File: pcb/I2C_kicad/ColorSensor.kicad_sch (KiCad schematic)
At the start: 0 parts

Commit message: started working on color sensor
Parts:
- added C2: 100nF, Capacitor_SMD:C_0603_1608Metric, symbol Device:C
- added R1, R2: 2.2kΩ, Resistor_SMD:R_0603_1608Metric, symbol Device:R
- added U1: VEML3328, SMD_L3328_VIS, symbol VEML3328:VEML3328
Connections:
- new net +3V3: C2.1, U1.4
- new net GND: C2.2, U1.1

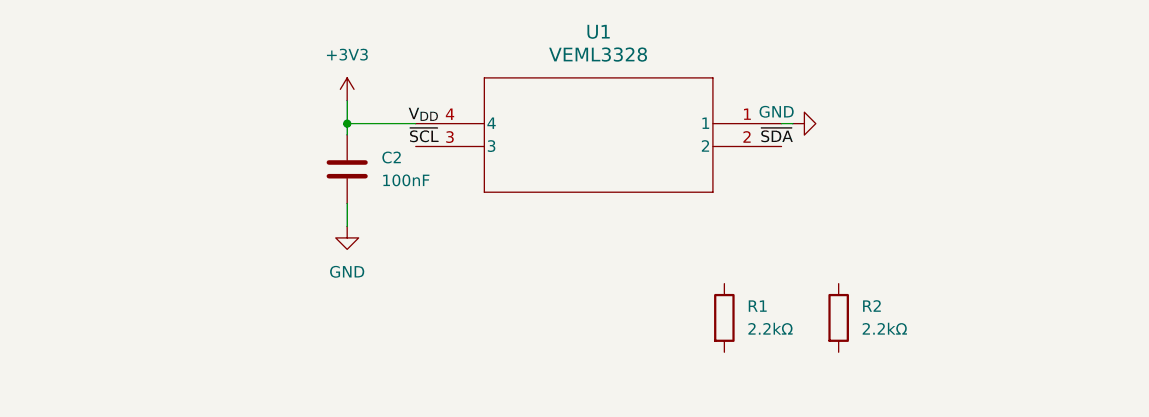
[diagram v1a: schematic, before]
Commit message: I worked on the color sensor and also the gpio expander. I added the pull ups for the SDA and SCL on the color sensor so no need to add any more. Just put do not populate for the other I2c devices
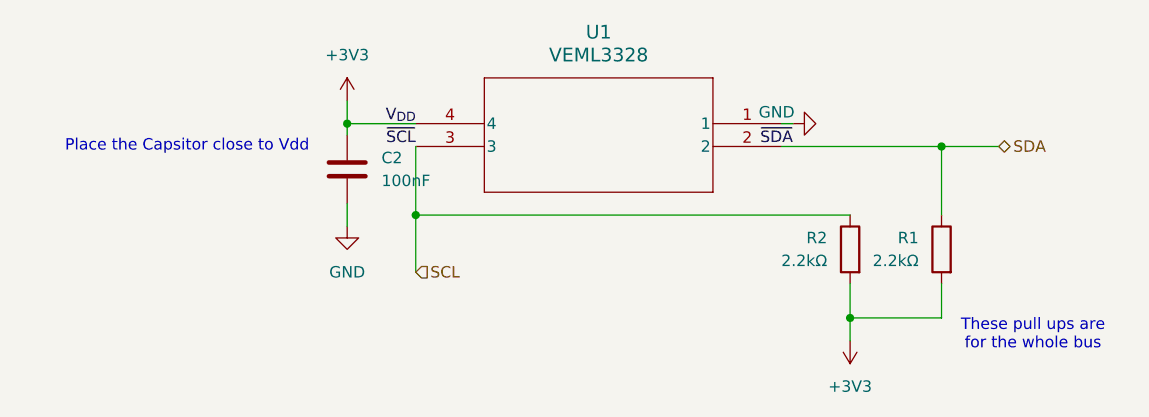
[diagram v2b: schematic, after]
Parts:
- U1: footprint SMD_L3328_VIS -> VEML3328:SMD_L3328_VIS; Manufacturer P/N 751-VEML3328TR-ND -> VEML3328
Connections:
- net +3V3: now also R1.2, R2.2
- net SDA: now reaches R1.1
- net SDA: now also U1.2
- net SCL: now reaches U1.3
- net SCL: now also R2.1
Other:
- note added: "Place the Capsitor close to Vdd"
- note added: "These pull ups are for the whole bus"
- company: (none) -> RoboCup
- title: (none) -> Color Sensor
- moved on the sheet: R1, R2

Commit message: Add IMU, Hall effect, and temp sensor sheets
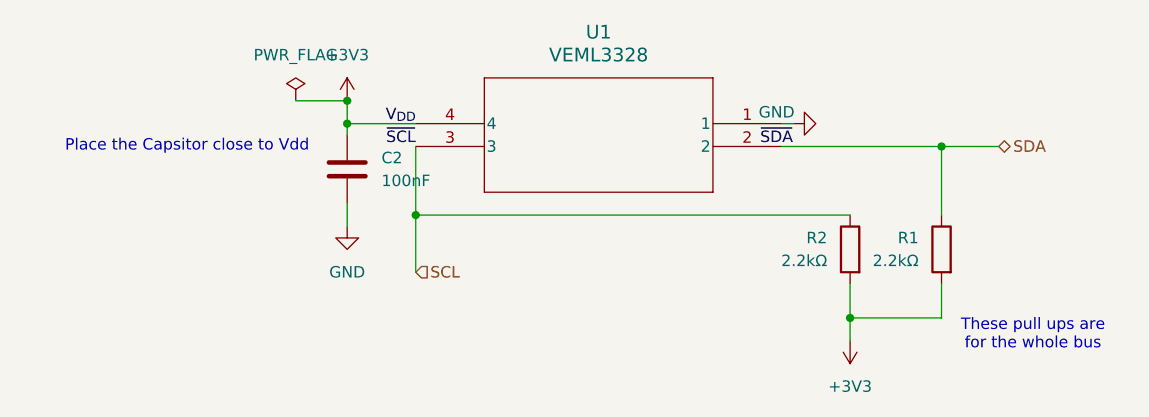
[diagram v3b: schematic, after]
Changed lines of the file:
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@@
+	)
+	(junction
+		(at 63.5 83.82)
+		(diameter 0)
+		(color 0 0 0 0)
 	)
 	(junction
@@
 		(pts
 			(xy 63.5 86.36) (xy 71.12 86.36)
+		)
+		(stroke
+			(width 0)
+			(type default)
+		)
+	)
+	(wire
+		(pts
+			(xy 57.785 83.82) (xy 63.5 83.82)
 		)
 		(stroke
@@
 					(unit 1)
 				)
+			)
+		)
+	)
+	(symbol
+		(lib_id "power:PWR_FLAG")
+		(at 57.785 83.82 0)
+		(unit 1)
+		(body_style 1)
+		(exclude_from_sim no)
+		(in_bom yes)
+		(on_board yes)
+		(in_pos_files yes)
+		(dnp no)
+		(fields_autoplaced yes)
+		(property "Reference" "#FLG01"
+			(at 57.785 81.915 0)
+			(hide yes)
+			(show_name no)
+			(do_not_autoplace no)
+			(effects
+				(font
+					(size 1.27 1.27)
+				)
+			)
+		)
+		(property "Value" "PWR_FLAG"
+			(at 57.785 78.74 0)
+			(show_name no)
+			(do_not_autoplace no)
+			(effects
+				(font
+					(size 1.27 1.27)
+				)
+			)
+		)
+		(property "Footprint" ""
+			(at 57.785 83.82 0)
+			(hide yes)
+			(show_name no)
+			(do_not_autoplace no)
+			(effects
+				(font
+					(size 1.27 1.27)
+				)
+			)
+		)
+		(property "Datasheet" ""
+			(at 57.785 83.82 0)
+			(hide yes)
+			(show_name no)
+			(do_not_autoplace no)
+			(effects
+				(font
+					(size 1.27 1.27)
+				)
+			)
+		)
+		(property "Description" "Special symbol for telling ERC where power comes from"
+			(at 57.785 83.82 0)
+			(hide yes)
+			(show_name no)
+			(do_not_autoplace no)
+			(effects
+				(font
+					(size 1.27 1.27)
+				)
+			)
+		)
+		(pin "1"
+		)
+		(instances
+			(project "I2C_kicad"
+				(path "/bea423eb-63f4-4e89-a865-e0d766357363/a483e119-e925-4b1f-adf6-c48d26119f2d"
+					(reference "#FLG01")
+					(unit 1)
+				)
